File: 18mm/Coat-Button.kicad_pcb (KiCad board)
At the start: 2 copper layers, 18 x 18 mm, 27 parts, among them IC1 MADW__ATTINY13-MM, P1 CONN_1, P2 CONN_1, P3 CONN_1, P4 CONN_1

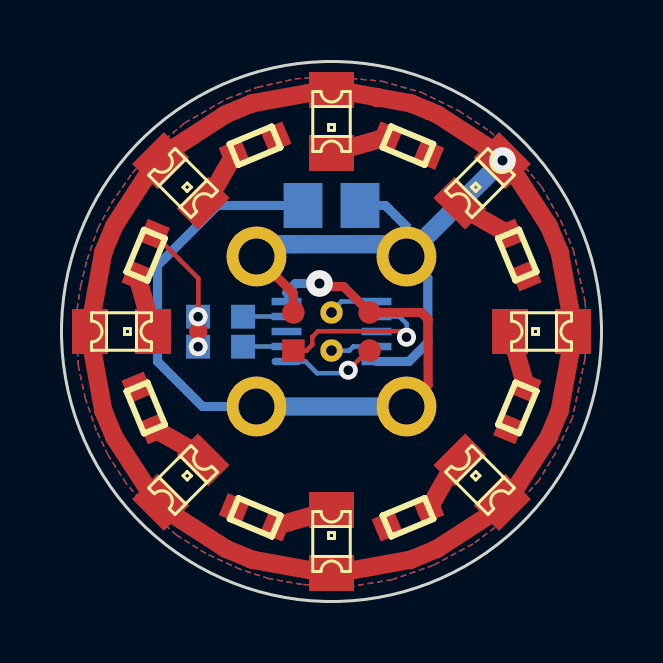
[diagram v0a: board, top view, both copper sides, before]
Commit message: Silkscreen tweaks.
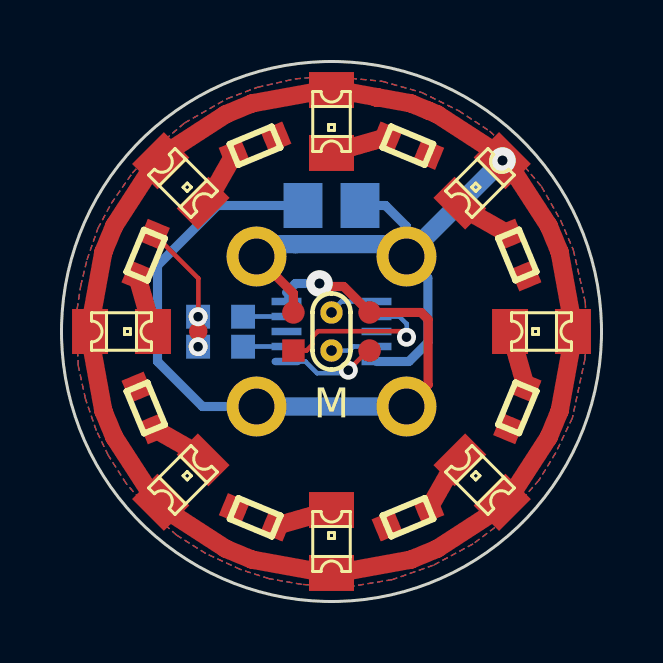
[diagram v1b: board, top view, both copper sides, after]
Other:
- board text added: "M"
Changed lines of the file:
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@@
     (area 65.303156 52.9 84.696844 75.100001)
     (thickness 1.6)
-    (drawings 12)
+    (drawings 13)
     (tracks 120)
     (zones 0)
@@
   )
   (layers
-    (15 F.Cu signal)
-    (0 B.Cu signal)
-    (18 B.Paste user)
-    (19 F.Paste user)
+    (15 F.Cu signal hide)
+    (0 B.Cu signal hide)
+    (18 B.Paste user hide)
+    (19 F.Paste user hide)
     (20 B.SilkS user)
     (21 F.SilkS user)
@@
     (mod_text_size 1.5 1.5)
     (mod_text_width 0.15)
-    (pad_size 1 1.5)
-    (pad_drill 0)
+    (pad_size 0.75 0.75)
+    (pad_drill 0.35)
     (pad_to_mask_clearance 0)
     (aux_axis_origin 0 0)
@@
     (add_net VCC)
   )
+  (module MADW__PIN_ARRAY_3x2_1.27mm (layer F.Cu)
+    (at 75 62)
+    (descr "Male 3x2 header with 1.27mm raster")
+    (tags "CONN, header, male, 3x2, 1.27mm")
+    (clearance 0.15)
+    (fp_text reference JP1 (at 0 -3.1) (layer F.SilkS) hide
+      (effects (font (size 1 1) (thickness 0.2)))
+    )
+    (fp_text value AVR_ISP (at 0 3.3) (layer F.SilkS) hide
+      (effects (font (size 1 1) (thickness 0.2)))
+    )
+    (fp_arc (start 0 -0.635) (end 0 -1.27) (angle 90) (layer F.SilkS) (width 0.15))
+    (fp_arc (start 0 -0.635) (end -0.635 -0.635) (angle 90) (layer F.SilkS) (width 0.15))
+    (fp_arc (start 0 0.635) (end 0 1.27) (angle 90) (layer F.SilkS) (width 0.15))
+    (fp_arc (start 0 0.635) (end 0.635 0.635) (angle 90) (layer F.SilkS) (width 0.15))
+    (fp_line (start 0.635 0.635) (end 0.635 -0.635) (layer F.SilkS) (width 0.15))
+    (fp_line (start -0.635 -0.635) (end -0.635 0.635) (layer F.SilkS) (width 0.15))
+    (pad 1 smd rect (at -1.27 0.635) (size 0.75 0.75)
+      (layers F.Cu F.Mask)
+      (net 3 MISO)
+    )
+    (pad 2 smd circle (at -1.27 -0.635) (size 0.75 0.75)
+      (layers F.Cu F.Mask)
+      (net 17 VCC)
+    )
+    (pad 3 thru_hole circle (at 0 0.635) (size 0.75 0.75) (drill 0.35)
+      (layers *.Cu F.Mask)
+      (net 16 SCK)
+    )
+    (pad 4 thru_hole circle (at 0 -0.635) (size 0.75 0.75) (drill 0.35)
+      (layers *.Cu F.Mask)
+      (net 4 MOSI)
+    )
+    (pad 5 smd circle (at 1.27 0.635) (size 0.75 0.75)
+      (layers F.Cu F.Mask)
+      (net 15 RST)
+    )
+    (pad 6 smd circle (at 1.27 -0.635) (size 0.75 0.75)
+      (layers F.Cu F.Mask)
+      (net 2 GND)
+    )
+  )
   (module MADW__MLF10 (layer B.Cu)
     (at 75 62)
@@
       (layers F.Cu F.Paste F.Mask)
       (net 8 N-0000014)
-    )
-  )
-  (module MADW__PIN_ARRAY_3x2_1.27mm (layer F.Cu)
-    (at 75 62)
-    (descr "Male 3x2 header with 1.27mm raster")
-    (tags "CONN, header, male, 3x2, 1.27mm")
-    (clearance 0.15)
-    (fp_text reference JP1 (at 0 -3.1) (layer F.SilkS) hide
-      (effects (font (size 1 1) (thickness 0.2)))
-    )
-    (fp_text value AVR_ISP (at 0 3.3) (layer F.SilkS) hide
-      (effects (font (size 1 1) (thickness 0.2)))
-    )
-    (pad 1 smd rect (at -1.27 0.635) (size 0.75 0.75)
-      (layers F.Cu F.Mask)
-      (net 3 MISO)
-    )
-    (pad 2 smd circle (at -1.27 -0.635) (size 0.75 0.75)
-      (layers F.Cu F.Mask)
-      (net 17 VCC)
-    )
-    (pad 3 thru_hole circle (at 0 0.635) (size 0.75 0.75) (drill 0.35)
-      (layers *.Cu F.Mask)
-      (net 16 SCK)
-    )
-    (pad 4 thru_hole circle (at 0 -0.635) (size 0.75 0.75) (drill 0.35)
-      (layers *.Cu F.Mask)
-      (net 4 MOSI)
-    )
-    (pad 5 smd circle (at 1.27 0.635) (size 0.75 0.75)
-      (layers F.Cu F.Mask)
-      (net 15 RST)
-    )
-    (pad 6 smd circle (at 1.27 -0.635) (size 0.75 0.75)
-      (layers F.Cu F.Mask)
-      (net 2 GND)
     )
   )
@@
       (xy 0.49276 -0.57404) (xy 0.52832 -0.56388) (xy 0.5334 -0.56388) (xy 0.5715 -0.56134)) (layer B.SilkS) (width 0.00254))
   )
+  (gr_text M (at 75 64.4) (layer F.SilkS)
+    (effects (font (size 1 1) (thickness 0.2)))
+  )
   (gr_line (start 70.6 60.1) (end 70.2 59.6) (angle 90) (layer B.SilkS) (width 0.2))
   (gr_line (start 71 59.6) (end 70.6 60.1) (angle 90) (layer B.SilkS) (width 0.2))
@@
     (effects (font (size 1 1) (thickness 0.2)) (justify mirror))
   )
-  (gr_text + (at 78.5876 60.6806) (layer B.SilkS)
+  (gr_text + (at 79.6 59.4) (layer B.SilkS)
     (effects (font (size 1.2 1.2) (thickness 0.2)) (justify mirror))
   )
-  (gr_text - (at 78.5114 63.119 90) (layer B.SilkS)
+  (gr_text - (at 79.5 64.5 180) (layer B.SilkS)
     (effects (font (size 1.2 1.2) (thickness 0.2)) (justify mirror))
   )

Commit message: Silkscreen tweaks.
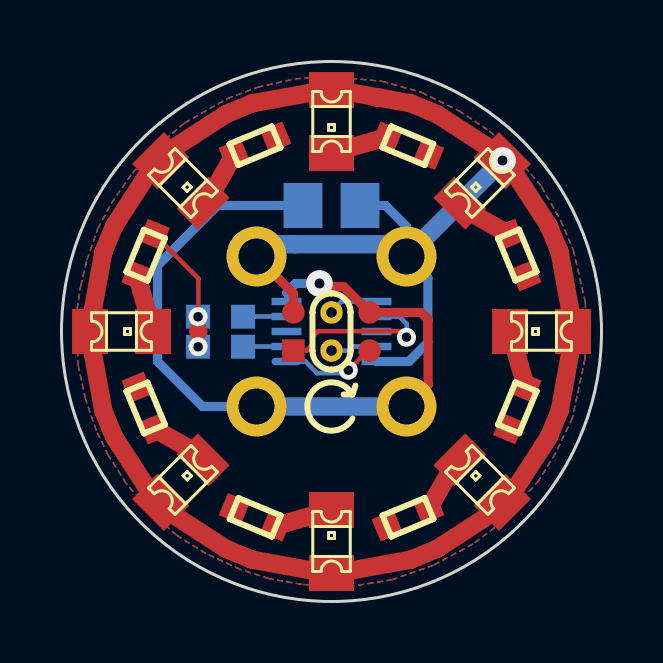
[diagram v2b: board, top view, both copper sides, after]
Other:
- board text removed: "M"
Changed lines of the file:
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@@
-(kicad_pcb (version 3) (host pcbnew "(2013-09-17 BZR 4321)-product")
+(kicad_pcb (version 3) (host pcbnew "(2013-09-18 BZR 4322)-product")
   (general
     (links 39)
@@
     (area 65.303156 52.9 84.696844 75.100001)
     (thickness 1.6)
-    (drawings 13)
+    (drawings 15)
     (tracks 120)
     (zones 0)
@@
   )
   (layers
-    (15 F.Cu signal hide)
-    (0 B.Cu signal hide)
-    (18 B.Paste user hide)
-    (19 F.Paste user hide)
+    (15 F.Cu signal)
+    (0 B.Cu signal)
+    (18 B.Paste user)
+    (19 F.Paste user)
     (20 B.SilkS user)
     (21 F.SilkS user)
@@
     (zone_45_only no)
     (trace_min 0.1524)
-    (segment_width 0.3048)
+    (segment_width 0.2)
     (edge_width 0.1)
     (via_size 0.635)
@@
     (pcb_text_width 0.3)
     (pcb_text_size 1.5 1.5)
-    (mod_edge_width 0.15)
+    (mod_edge_width 0.2)
     (mod_text_size 1.5 1.5)
     (mod_text_width 0.15)
@@
       (effects (font (size 1 1) (thickness 0.2)))
     )
-    (fp_arc (start 0 -0.635) (end 0 -1.27) (angle 90) (layer F.SilkS) (width 0.15))
-    (fp_arc (start 0 -0.635) (end -0.635 -0.635) (angle 90) (layer F.SilkS) (width 0.15))
-    (fp_arc (start 0 0.635) (end 0 1.27) (angle 90) (layer F.SilkS) (width 0.15))
-    (fp_arc (start 0 0.635) (end 0.635 0.635) (angle 90) (layer F.SilkS) (width 0.15))
-    (fp_line (start 0.635 0.635) (end 0.635 -0.635) (layer F.SilkS) (width 0.15))
-    (fp_line (start -0.635 -0.635) (end -0.635 0.635) (layer F.SilkS) (width 0.15))
+    (fp_arc (start 0 -0.635) (end 0 -1.27) (angle 90) (layer F.SilkS) (width 0.2))
+    (fp_arc (start 0 -0.635) (end -0.635 -0.635) (angle 90) (layer F.SilkS) (width 0.2))
+    (fp_arc (start 0 0.635) (end 0 1.27) (angle 90) (layer F.SilkS) (width 0.2))
+    (fp_arc (start 0 0.635) (end 0.635 0.635) (angle 90) (layer F.SilkS) (width 0.2))
+    (fp_line (start 0.635 0.635) (end 0.635 -0.635) (layer F.SilkS) (width 0.2))
+    (fp_line (start -0.635 -0.635) (end -0.635 0.635) (layer F.SilkS) (width 0.2))
     (pad 1 smd rect (at -1.27 0.635) (size 0.75 0.75)
       (layers F.Cu F.Mask)
@@
       (xy 0.49276 -0.57404) (xy 0.52832 -0.56388) (xy 0.5334 -0.56388) (xy 0.5715 -0.56134)) (layer B.SilkS) (width 0.00254))
   )
-  (gr_text M (at 75 64.4) (layer F.SilkS)
-    (effects (font (size 1 1) (thickness 0.2)))
-  )
+  (gr_line (start 75.7 64.1) (end 75.4 64.1) (angle 90) (layer F.SilkS) (width 0.2))
+  (gr_line (start 75.7 64.1) (end 75.8 63.8) (angle 90) (layer F.SilkS) (width 0.2))
+  (gr_arc (start 75 64.5) (end 75.7 64.9) (angle 290) (layer F.SilkS) (width 0.2))
   (gr_line (start 70.6 60.1) (end 70.2 59.6) (angle 90) (layer B.SilkS) (width 0.2))
   (gr_line (start 71 59.6) (end 70.6 60.1) (angle 90) (layer B.SilkS) (width 0.2))
